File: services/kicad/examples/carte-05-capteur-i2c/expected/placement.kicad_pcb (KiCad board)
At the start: 2 copper layers, 26 parts, among them J1 IN_5V, J2 SWD, J3 I2C, U1 STM32F103C8T6, U2 AMS1117-3.3, U3 BME280

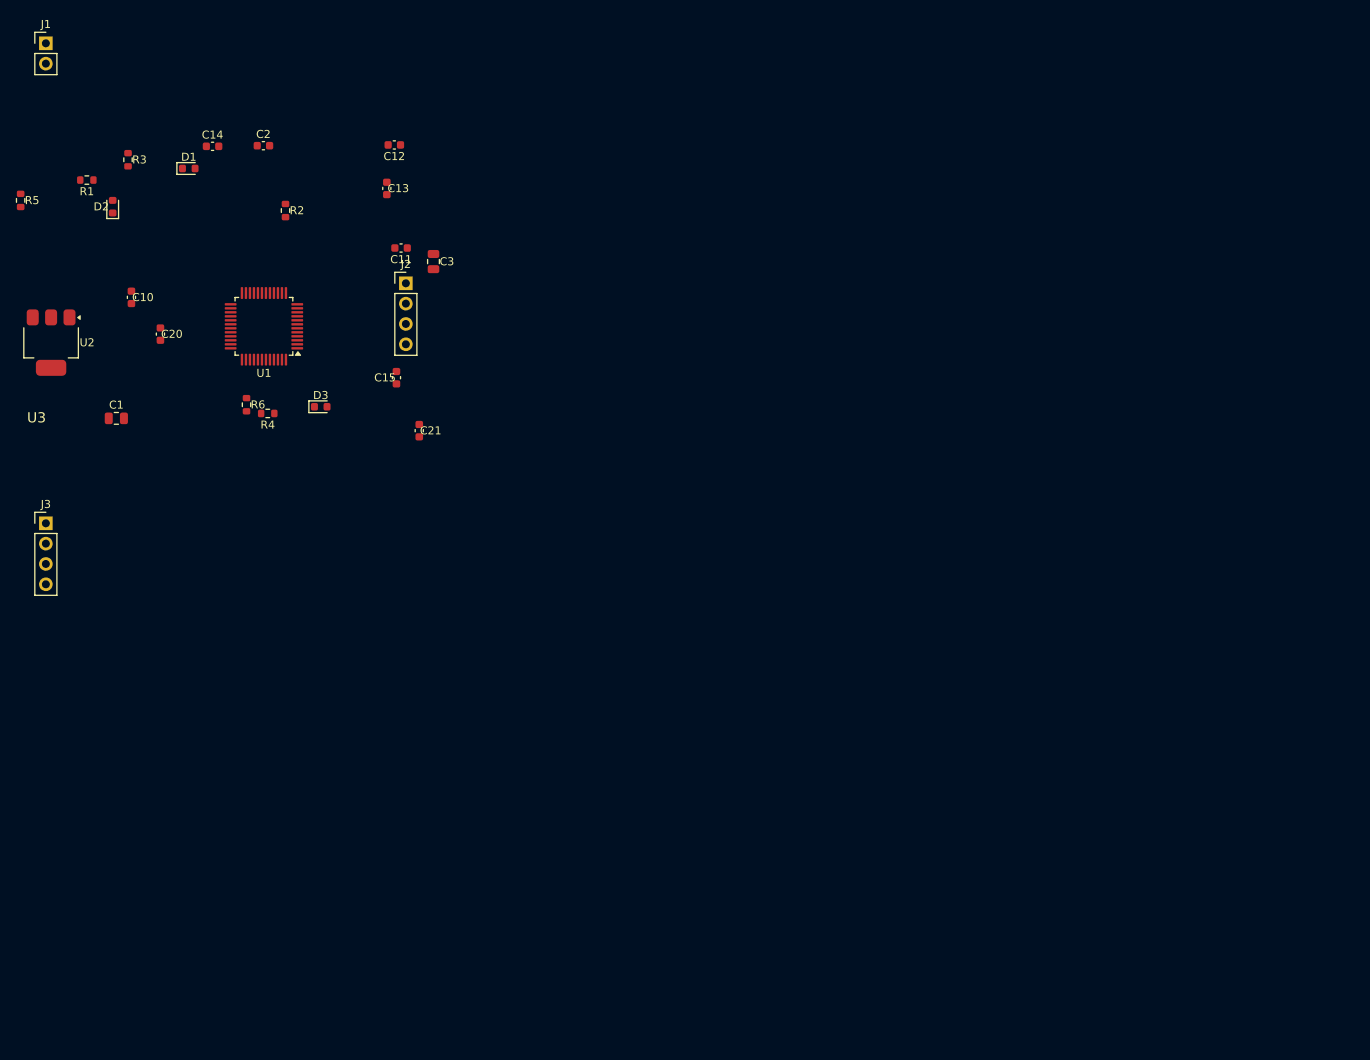
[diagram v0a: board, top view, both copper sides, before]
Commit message: fix(pcb): le composant perdu avait une raison, et la lib la rendait depuis toujours
« Pourquoi le niveau 1 perd le BME280 ? » — la question de l utilisateur, et je
l avais contournee sans y repondre. Mes propres notes affirmaient que
`place_all_components` « n emet AUCUN message, meme en journalisation DEBUG ».

C etait vrai de ses JOURNAUX. C etait faux de ce qu elle REND :

    RESULTAT places=25 echoues=1
       ECHEC U3 -> Failed to add footprint

Elle enregistre chaque echec, avec sa raison, dans `result.failed`. Nous jetions
la valeur de retour.

⚠️ SEPTIEME FOIS QUE CE DEPOT PAIE « NE PAS LIRE CE QUE LA LIB REND », apres
`FunctionalCluster.max_distance_mm`, `anchor_pin`, `WorkflowConfig.grid`,
`constraints=`, `PCB.move_reference` et `bottom_up_placement`. Les six premieres
etaient des leviers non appeles ; celle-ci est un DIAGNOSTIC non lu, et elle a
coute deux jours de recherche pour une reponse disponible en une ligne.

LA CAUSE

    demande   Package_LGA:LGA-8_2.5x2.5mm_P0.65mm
    existe    Package_LGA:Bosch_LGA-8_2.5x2.5mm_P0.65mm_ClockwisePinNumbering

KiCad livre l empreinte du BME280 prefixee `Bosch_` et suffixee
`_ClockwisePinNumbering` — ce capteur numerote ses broches dans le sens horaire,
contrairement a la convention LGA. `add_component` rendait `None`.

⚠️ J avais ecrit que « le symbole ET l empreinte existent tous deux ». Je l avais
verifie sur le SYMBOLE `Sensor:BME280`, jamais sur l empreinte. Verifier a cote
de la question compte pour ne pas avoir verifie.

DEUX CORRECTIFS

1. `tools/pcb.py` journalise desormais chaque `failed` et chaque `warning` de
   `place_all_components`. Le prochain composant perdu se nommera lui-meme.
   On ne LEVE pas : la cascade sait retomber, et `_composants_perdus` refuse
   deja le board incomplet. Mais un echec qui ne se nomme pas se rediagnostique
   a chaque fois.

2. L empreinte de `carte-05` corrigee vers le nom reel.

RESULTAT MESURE

    niveau 1 a PERDU 1 composant(s) (U3)     <- avant
    niveau 1 kicad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
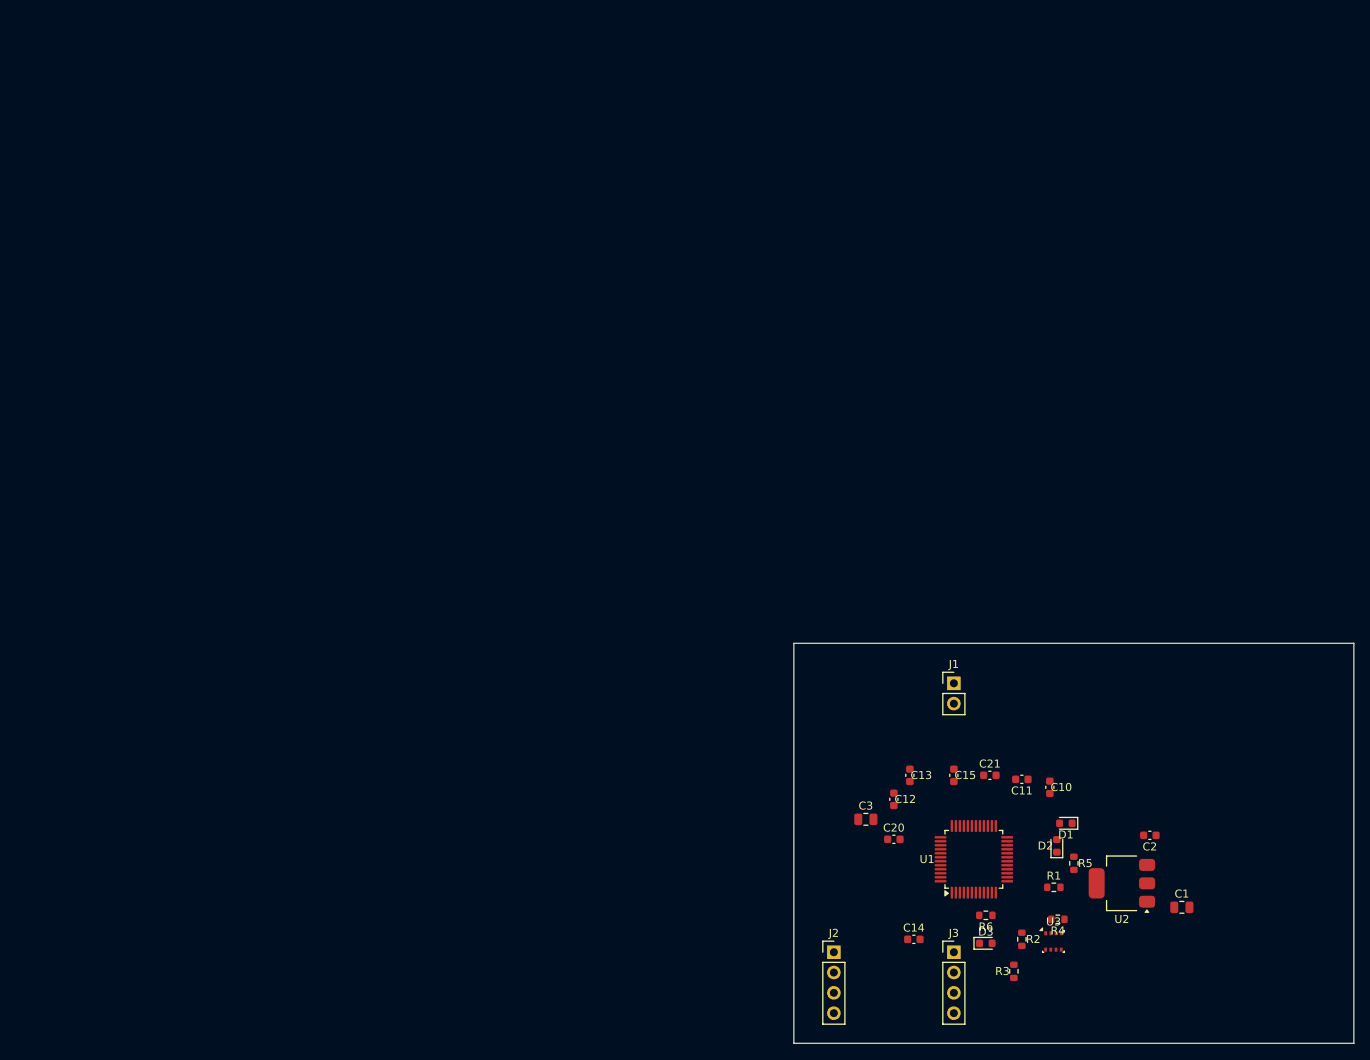
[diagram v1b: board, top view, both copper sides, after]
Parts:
- U3: footprint (none) -> Bosch_LGA-8_2.5x2.5mm_P0.65mm_ClockwisePinNumbering
- moved R5 155.6 mm to (148.5, 107.5)
- moved R3 150.2 mm to (141.0, 121.0), turned to 90 degrees
- moved U2 149.9 mm to (154.5, 110.0), turned to 180 degrees
- moved R1 149.8 mm to (146.0, 110.5), turned to 0 degrees
- moved C1 146.5 mm to (162.0, 113.0)
- moved U3 143.0 mm to (145.9, 117.3)
- moved D2 142.5 mm to (146.4, 105.3)
- moved C2 140.4 mm to (158.0, 104.0), turned to 180 degrees
- moved J1 138.9 mm to (133.5, 85.0)
- moved D1 136.8 mm to (147.5, 102.5), turned to 180 degrees
- moved C14 132.3 mm to (128.5, 117.0)
- moved C10 130.1 mm to (145.5, 98.0)
- moved R2 129.5 mm to (142.0, 117.0)
- moved J3 125.5 mm to (133.5, 118.6)
- moved R4 117.3 mm to (146.5, 114.5)
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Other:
- board outline added: 70 x 50 mm

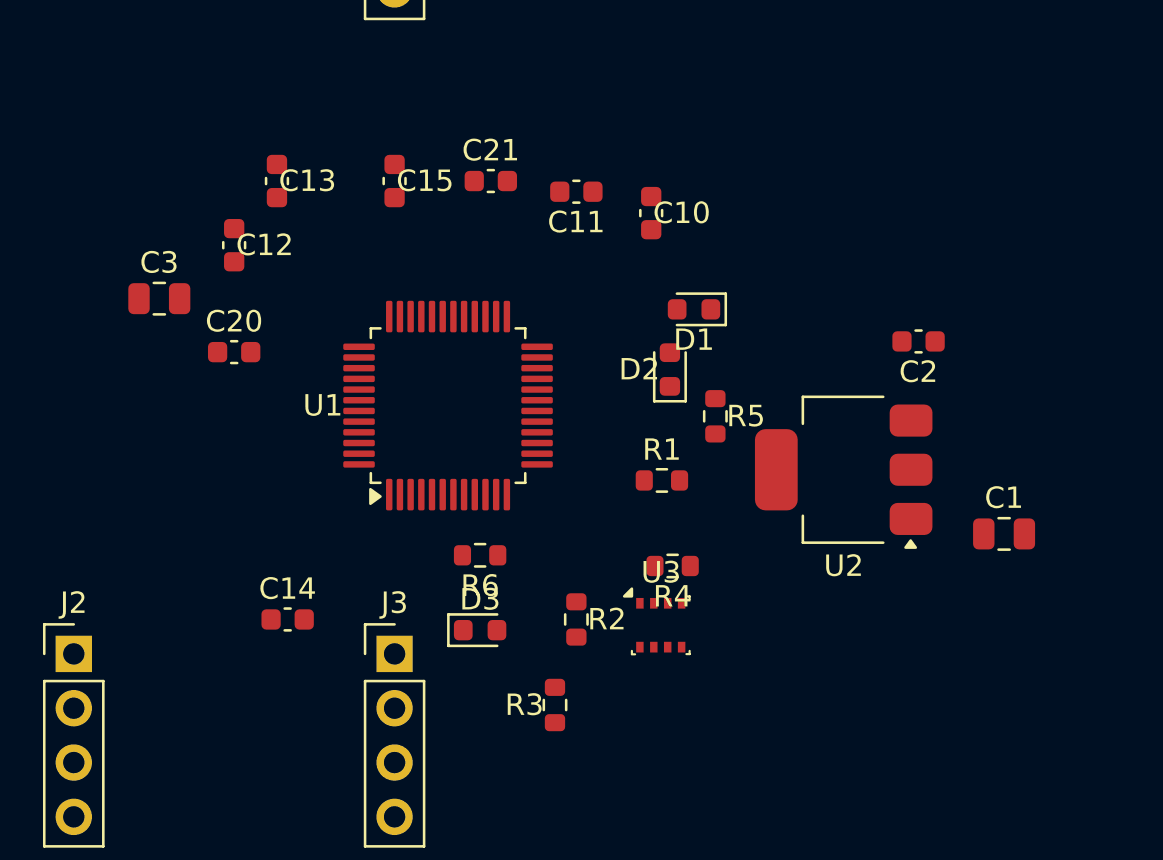
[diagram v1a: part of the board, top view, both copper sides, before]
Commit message: feat(examples): carte-05 livree avec le decouplage corrige ; mesures.json suit la livraison
carte-05 : 100 % / 0 erreur DRC / fabricable, decouplage corps->broche
7,1 -> 3,6 mm (capas reattribuees au CI le plus proche sur leur rail, snap
sur la broche). Placement livre a cote du board route.

livrer_campagne.py ecrit desormais mesures.json depuis la ligne SUMMARY et
le DRC du conteneur : la carte gardait la mesure de la livraison precedente
(38 violations pour un board a 59), et le script lit ce fichier dans git
pour juger la campagne suivante.

Co-Authored-By: Claude Fable 5.1 <noreply@anthropic.com>
Claude-Session: https://claude.ai/code/session_01TnMqm4La2CxQHHB5K8aSSV
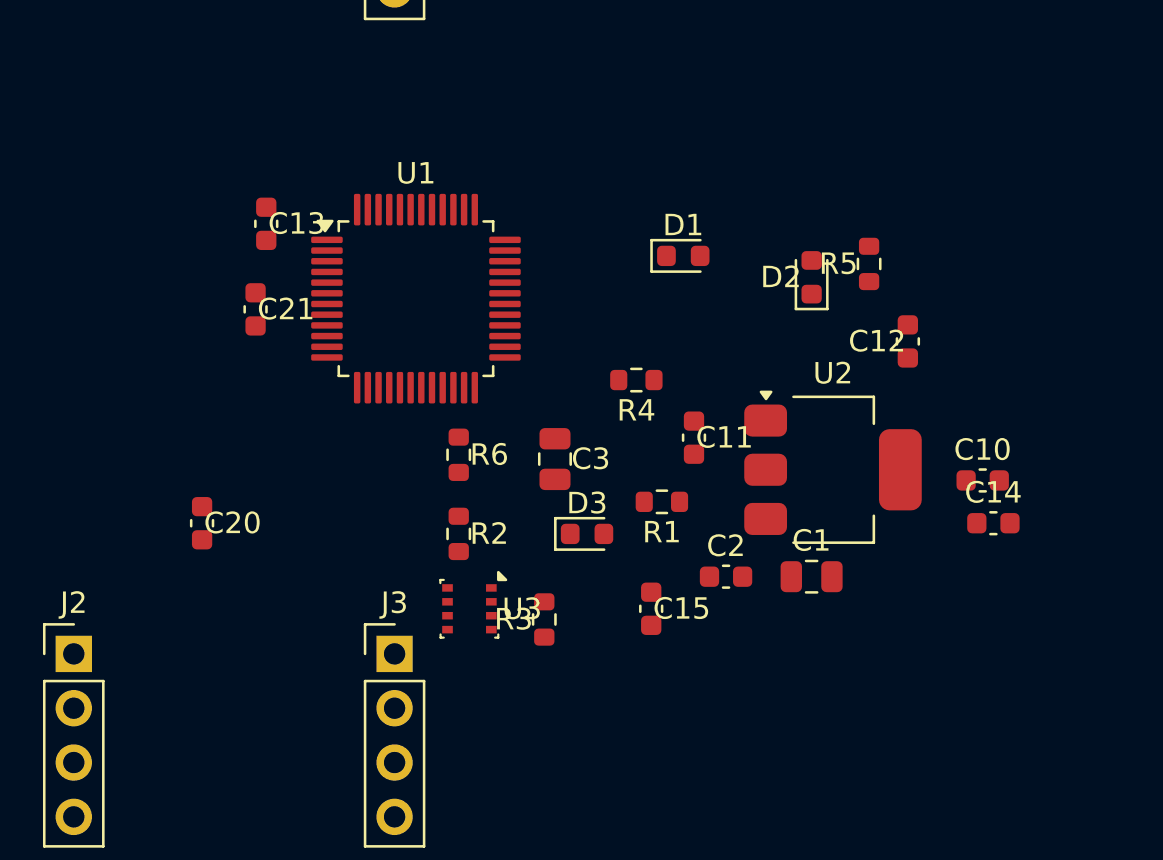
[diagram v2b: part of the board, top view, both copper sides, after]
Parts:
- moved C14 33.3 mm to (161.5, 112.5)
- moved C12 31.8 mm to (157.5, 104.0), turned to 90 degrees
- moved C15 23.3 mm to (145.5, 116.5)
- moved C3 20.0 mm to (141.0, 109.5), turned to 270 degrees
- moved C10 19.9 mm to (161.0, 110.5), turned to 0 degrees
- moved C2 14.2 mm to (149.0, 115.0), turned to 0 degrees
- moved C11 12.7 mm to (147.5, 108.5), turned to 270 degrees
- moved C21 12.5 mm to (127.0, 102.5), turned to 270 degrees
- moved R5 10.1 mm to (155.7, 100.4), turned to 90 degrees
- moved C1 9.22 mm to (153.0, 115.0)
- moved U3 8.98 mm to (137.0, 116.5), turned to 270 degrees
- moved R4 8.86 mm to (144.8, 105.8)
- moved C20 8.14 mm to (124.5, 112.5), turned to 270 degrees
- moved D2 7.91 mm to (153.0, 101.0)
- moved R2 6.80 mm to (136.5, 113.0)
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
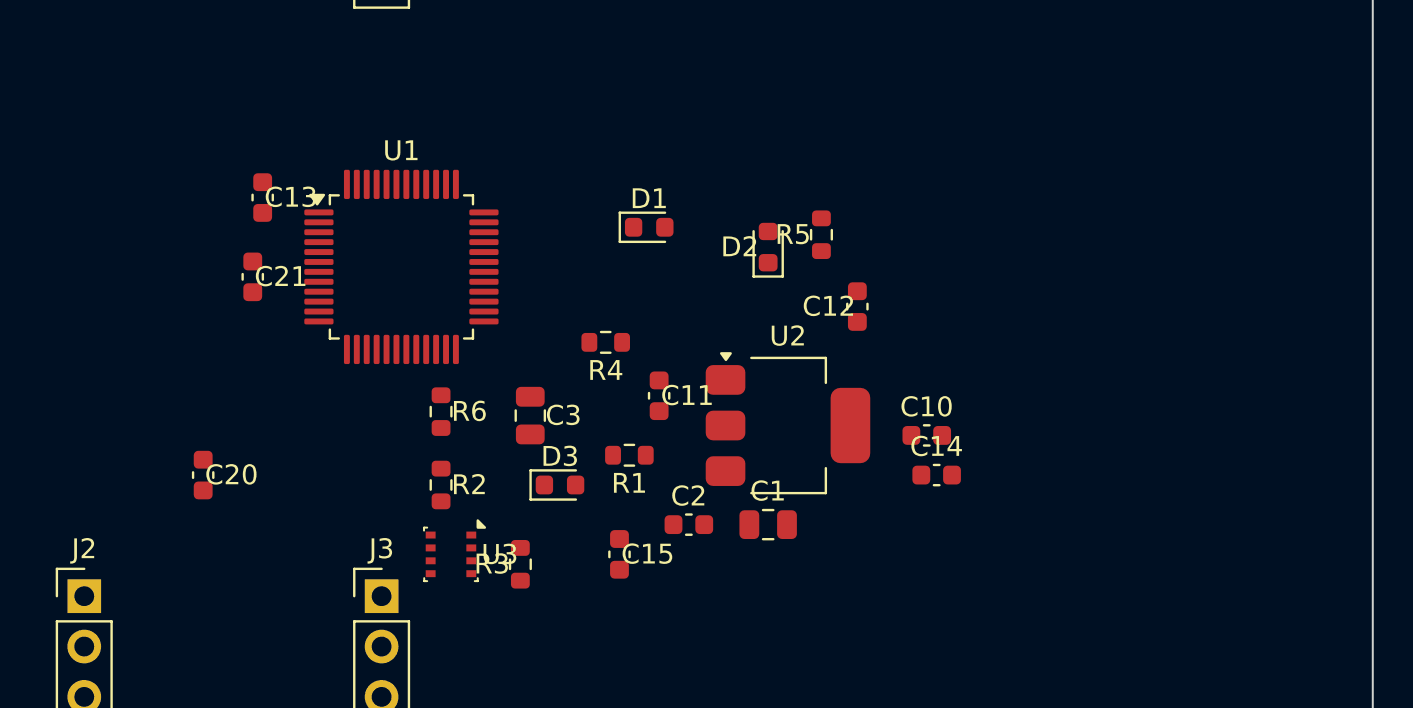
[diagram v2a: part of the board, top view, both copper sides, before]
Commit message: examples: carte-01 a 07 -- placement valide et gele (phase 1) puis route dessus (phase 2) : 100 %, 0 erreur, 2 couches
Sequence en deux phases demandee par l'utilisateur : valider_placements.py (critere pro : chaque broche VDD a sa capa a <= 3,5 mm) puis banc_exemples.py --placement-fige. 30 s a 2,6 min de routage par carte.

Co-Authored-By: Claude Fable 5.1 <noreply@anthropic.com>

Claude-Session: https://claude.ai/code/session_01TnMqm4La2CxQHHB5K8aSSV
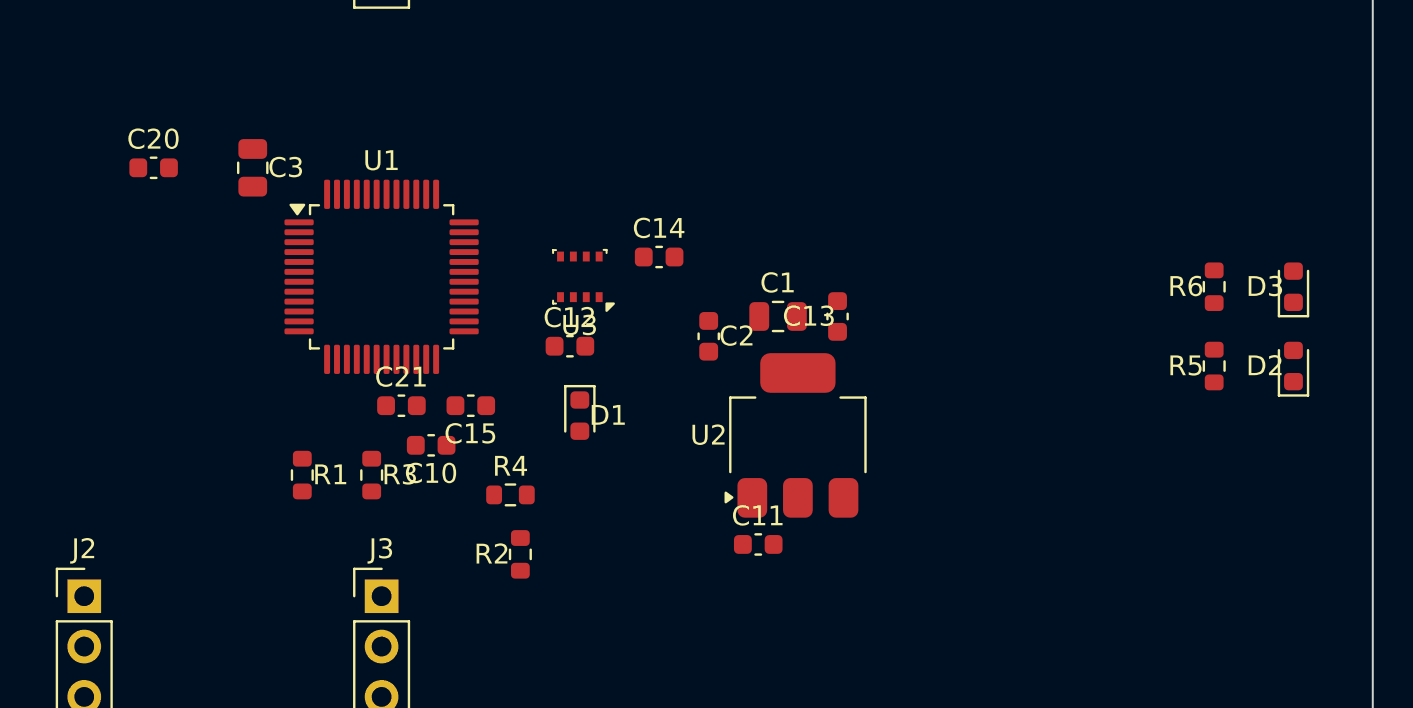
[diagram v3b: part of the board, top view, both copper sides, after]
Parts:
- moved R6 39.5 mm to (175.5, 103.0), turned to 90 degrees
- moved D3 38.3 mm to (179.5, 103.0), turned to 90 degrees
- moved C13 29.6 mm to (156.5, 104.5), turned to 90 degrees
- moved D2 27.2 mm to (179.5, 107.0)
- moved C10 25.0 mm to (136.0, 111.0), turned to 180 degrees
- moved R5 20.9 mm to (175.5, 107.0)
- moved C3 18.8 mm to (127.0, 97.0)
- moved C14 17.8 mm to (147.5, 101.5)
- moved R1 16.5 mm to (129.5, 112.5), turned to 270 degrees
- moved C20 15.7 mm to (122.0, 97.0), turned to 0 degrees
- moved U3 15.4 mm to (143.5, 102.5), turned to 180 degrees
- moved C12 14.6 mm to (143.0, 106.0), turned to 0 degrees
- moved C15 10.6 mm to (138.0, 109.0), turned to 180 degrees
- moved C1 10.5 mm to (153.5, 104.5)
- moved D1 10.1 mm to (143.5, 109.5), turned to 270 degrees
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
